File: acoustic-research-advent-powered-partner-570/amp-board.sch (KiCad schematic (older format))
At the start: 3 parts

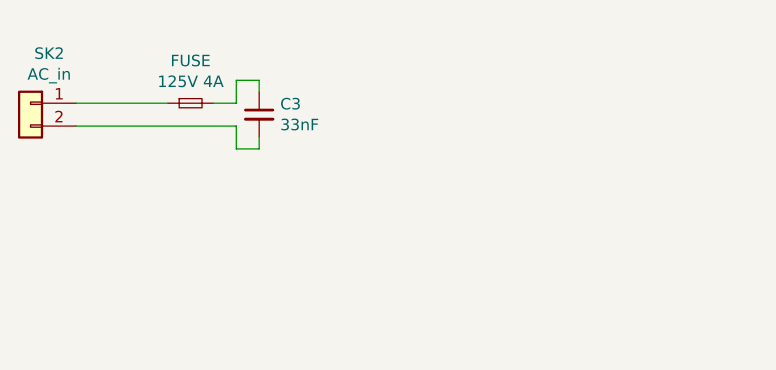
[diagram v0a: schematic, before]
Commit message: starting on the power input circuits
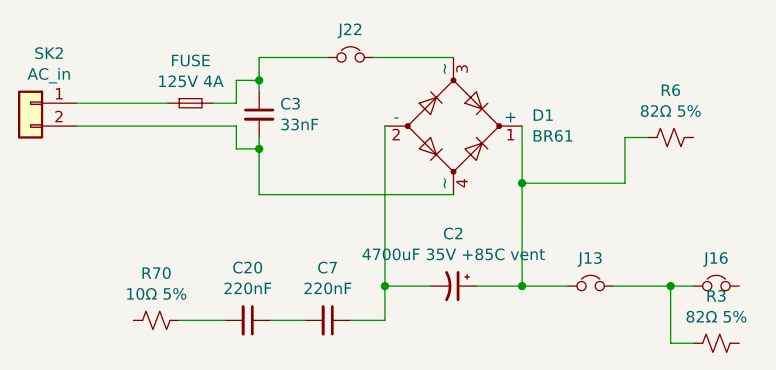
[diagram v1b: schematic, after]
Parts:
- added C2: 4700uF 35V +85C vent, symbol Device:CP1_Small
- added C20, C7: 220nF, symbol Device:C_Small
- added D1: BR61, symbol Device:D_Bridge_+-AA
- added J13, J16, J22: ~, symbol Device:Jumper_NC_Small
- added R3, R6: 82Ω 5%, symbol Device:R_Small_US
- added R70: 10Ω 5%, symbol Device:R_Small_US
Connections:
- net at C3.2, SK2.2 (Pin_2): now also D1.4 (~~)
- net at C3.1, FUSE.2: now also J22.1
- new net: C2.1, D1.1 (+), J13.1, R6.2
- new net: C2.2, C7.1, D1.2 (-)
- new net: D1.3 (~~), J22.2
- new net: C20.1, C7.2
- new net: J13.2, J16.1, R3.2
- new net: C20.2, R70.1
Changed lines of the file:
@@
 Wire Wire Line
 	1950 1500 1950 1450
+$Comp
+L Device:D_Bridge_+-AA D1
+U 1 1 5E8D387E
+P 2800 1400
+F 0 "D1" H 3144 1446 50  0000 L CNN
+F 1 "BR61" H 3144 1355 50  0000 L CNN
+F 2 "" H 2800 1400 50  0001 C CNN
+F 3 "~" H 2800 1400 50  0001 C CNN
+	1    2800 1400
+	1    0    0    -1
+$EndComp
+Wire Wire Line
+	1950 1200 1950 1100
+Wire Wire Line
+	1950 1100 2250 1100
+Connection ~ 1950 1200
+Wire Wire Line
+	1950 1500 1950 1700
+Wire Wire Line
+	1950 1700 2800 1700
+Connection ~ 1950 1500
+$Comp
+L Device:Jumper_NC_Small J22
+U 1 1 5E8D4B72
+P 2350 1100
+F 0 "J22" H 2350 1221 50  0000 C CNN
+F 1 "~" H 2350 1221 50  0000 C CNN
+F 2 "" H 2350 1100 50  0001 C CNN
+F 3 "~" H 2350 1100 50  0001 C CNN
+	1    2350 1100
+	1    0    0    -1
+$EndComp
+Wire Wire Line
+	2450 1100 2800 1100
+$Comp
+L Device:CP1_Small C2
+U 1 1 5E8D52A8
+P 2800 2100
+F 0 "C2" V 2572 2100 50  0000 C CNN
+F 1 "4700uF 35V +85C vent" V 2663 2100 50  0000 C CNN
+F 2 "" H 2800 2100 50  0001 C CNN
+F 3 "~" H 2800 2100 50  0001 C CNN
+	1    2800 2100
+	0    1    1    0
+$EndComp
+Wire Wire Line
+	2500 1400 2500 2100
+Wire Wire Line
+	2500 2100 2700 2100
+Wire Wire Line
+	3100 1400 3100 1650
+Wire Wire Line
+	3100 2100 2900 2100
+$Comp
+L Device:C_Small C7
+U 1 1 5E8D755A
+P 2250 2250
+F 0 "C7" V 2021 2250 50  0000 C CNN
+F 1 "220nF" V 2112 2250 50  0000 C CNN
+F 2 "" H 2250 2250 50  0001 C CNN
+F 3 "~" H 2250 2250 50  0001 C CNN
+	1    2250 2250
+	0    1    1    0
+$EndComp
+Wire Wire Line
+	2500 2100 2500 2250
+Wire Wire Line
+	2500 2250 2350 2250
+Connection ~ 2500 2100
+$Comp
+L Device:R_Small_US R6
+U 1 1 5E8D7F49
+P 3750 1450
+F 0 "R6" V 3545 1450 50  0000 C CNN
+F 1 "82Ω 5%" V 3636 1450 50  0000 C CNN
+F 2 "" H 3750 1450 50  0001 C CNN
+F 3 "~" H 3750 1450 50  0001 C CNN
+	1    3750 1450
+	0    1    1    0
+$EndComp
+Wire Wire Line
+	3100 1650 3550 1650
+Wire Wire Line
+	3550 1650 3550 1450
+Wire Wire Line
+	3550 1450 3650 1450
+Connection ~ 3100 1650
+Wire Wire Line
+	3100 1650 3100 2100
+$Comp
+L Device:Jumper_NC_Small J13
+U 1 1 5E8D8BA6
+P 3400 2100
+F 0 "J13" H 3400 2221 50  0000 C CNN
+F 1 "~" H 3400 2221 50  0000 C CNN
+F 2 "" H 3400 2100 50  0001 C CNN
+F 3 "~" H 3400 2100 50  0001 C CNN
+	1    3400 2100
+	1    0    0    -1
+$EndComp
+Wire Wire Line
+	3100 2100 3300 2100
+Connection ~ 3100 2100
+$Comp
+L Device:C_Small C20
+U 1 1 5E8D9A58
+P 1900 2250
+F 0 "C20" V 1671 2250 50  0000 C CNN
+F 1 "220nF" V 1762 2250 50  0000 C CNN
+F 2 "" H 1900 2250 50  0001 C CNN
+F 3 "~" H 1900 2250 50  0001 C CNN
+	1    1900 2250
+	0    1    1    0
+$EndComp
+Wire Wire Line
+	2000 2250 2150 2250
+$Comp
+L Device:R_Small_US R70
+U 1 1 5E8DA32F
+P 1500 2250
+F 0 "R70" V 1295 2250 50  0000 C CNN
+F 1 "10Ω 5%" V 1386 2250 50  0000 C CNN
+F 2 "" H 1500 2250 50  0001 C CNN
+F 3 "~" H 1500 2250 50  0001 C CNN
+	1    1500 2250
+	0    1    1    0
+$EndComp
+Wire Wire Line
+	1600 2250 1800 2250
+$Comp
+L Device:Jumper_NC_Small J16
+U 1 1 5E8DAF35
+P 3950 2100
+F 0 "J16" H 3950 2221 50  0000 C CNN
+F 1 "~" H 3950 2221 50  0000 C CNN
+F 2 "" H 3950 2100 50  0001 C CNN
+F 3 "~" H 3950 2100 50  0001 C CNN
+	1    3950 2100
+	1    0    0    -1
+$EndComp
+$Comp
+L Device:R_Small_US R3
+U 1 1 5E8DB2C5
+P 3950 2350
+F 0 "R3" V 3745 2350 50  0000 C CNN
+F 1 "82Ω 5%" V 3836 2350 50  0000 C CNN
+F 2 "" H 3950 2350 50  0001 C CNN
+F 3 "~" H 3950 2350 50  0001 C CNN
+	1    3950 2350
+	0    1    1    0
+$EndComp
+Wire Wire Line
+	3850 2100 3750 2100
+Wire Wire Line
+	3750 2100 3750 2350
+Wire Wire Line
+	3750 2350 3850 2350
+Wire Wire Line
+	3500 2100 3750 2100
+Connection ~ 3750 2100
 $EndSCHEMATC

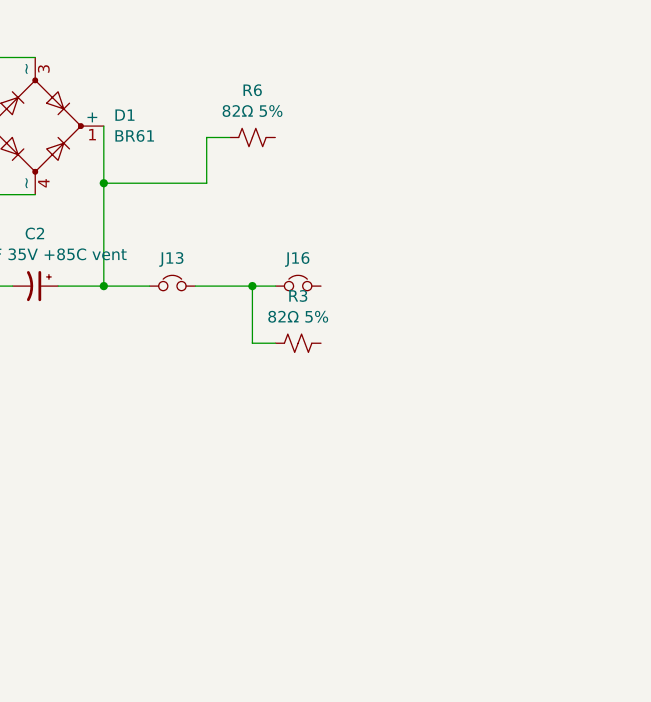
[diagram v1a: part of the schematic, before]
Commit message: more transistors
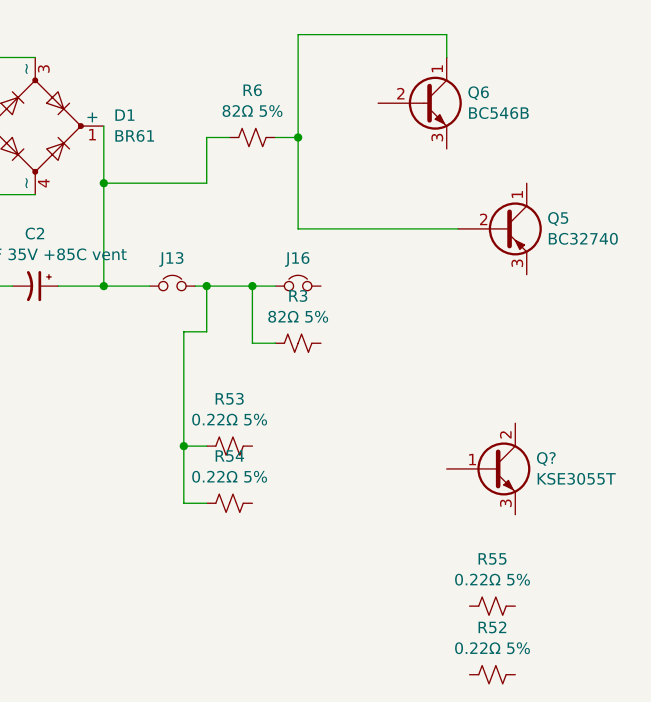
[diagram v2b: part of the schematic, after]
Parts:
- added Q5: BC32740, Package_TO_SOT_THT:TO-92_Inline, symbol Transistor_BJT:BC327
- added Q6: BC546B, Package_TO_SOT_THT:TO-92_Inline, symbol Transistor_BJT:BC546
- added Q?: KSE3055T, symbol Device:Q_NPN_BCE
- added R52, R53, R54, R55: 0.22Ω 5%, symbol Device:R_Small_US
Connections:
- net at R6.1: now also Q5.2 (B), Q6.1 (C)
- net at J13.2, J16.1, R3.2: now also R53.2, R54.2
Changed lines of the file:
@@
 	3750 2350 3850 2350
 Wire Wire Line
-	3500 2100 3750 2100
+	3500 2100 3550 2100
 Connection ~ 3750 2100
+$Comp
+L Transistor_BJT:BC546 Q6
+U 1 1 5E8DC9B8
+P 4500 1300
+F 0 "Q6" H 4691 1346 50  0000 L CNN
+F 1 "BC546B" H 4691 1255 50  0000 L CNN
+F 2 "Package_TO_SOT_THT:TO-92_Inline" H 4700 1225 50  0001 L CIN
+F 3 "http://www.fairchildsemi.com/ds/BC/BC547.pdf" H 4500 1300 50  0001 L CNN
+	1    4500 1300
+	1    0    0    -1
+$EndComp
+Wire Wire Line
+	3850 1450 3950 1450
+Wire Wire Line
+	3950 1450 3950 1000
+Wire Wire Line
+	3950 1000 4600 1000
+Wire Wire Line
+	4600 1000 4600 1100
+$Comp
+L Transistor_BJT:BC327 Q5
+U 1 1 5E8DDD31
+P 4850 1850
+F 0 "Q5" H 5040 1896 50  0000 L CNN
+F 1 "BC32740" H 5040 1805 50  0000 L CNN
+F 2 "Package_TO_SOT_THT:TO-92_Inline" H 5050 1775 50  0001 L CIN
+F 3 "http://www.onsemi.com/pub_link/Collateral/BC327-D.PDF" H 4850 1850 50  0001 L CNN
+	1    4850 1850
+	1    0    0    -1
+$EndComp
+Wire Wire Line
+	3950 1450 3950 1850
+Wire Wire Line
+	3950 1850 4650 1850
+Connection ~ 3950 1450
+$Comp
+L Device:R_Small_US R53
+U 1 1 5E8DEE3E
+P 3650 2800
+F 0 "R53" V 3445 2800 50  0000 C CNN
+F 1 "0.22Ω 5%" V 3536 2800 50  0000 C CNN
+F 2 "" H 3650 2800 50  0001 C CNN
+F 3 "~" H 3650 2800 50  0001 C CNN
+	1    3650 2800
+	0    1    1    0
+$EndComp
+$Comp
+L Device:R_Small_US R54
+U 1 1 5E8DF44C
+P 3650 3050
+F 0 "R54" V 3445 3050 50  0000 C CNN
+F 1 "0.22Ω 5%" V 3536 3050 50  0000 C CNN
+F 2 "" H 3650 3050 50  0001 C CNN
+F 3 "~" H 3650 3050 50  0001 C CNN
+	1    3650 3050
+	0    1    1    0
+$EndComp
+$Comp
+L Device:R_Small_US R55
+U 1 1 5E8DFA91
+P 4800 3500
+F 0 "R55" V 4595 3500 50  0000 C CNN
+F 1 "0.22Ω 5%" V 4686 3500 50  0000 C CNN
+F 2 "" H 4800 3500 50  0001 C CNN
+F 3 "~" H 4800 3500 50  0001 C CNN
+	1    4800 3500
+	0    1    1    0
+$EndComp
+$Comp
+L Device:R_Small_US R52
+U 1 1 5E8DFF45
+P 4800 3800
+F 0 "R52" V 4595 3800 50  0000 C CNN
+F 1 "0.22Ω 5%" V 4686 3800 50  0000 C CNN
+F 2 "" H 4800 3800 50  0001 C CNN
+F 3 "~" H 4800 3800 50  0001 C CNN
+	1    4800 3800
+	0    1    1    0
+$EndComp
+Wire Wire Line
+	3550 2800 3450 2800
+Wire Wire Line
+	3450 2800 3450 3050
+Wire Wire Line
+	3450 3050 3550 3050
+Wire Wire Line
+	3450 2800 3450 2300
+Wire Wire Line
+	3450 2300 3550 2300
+Wire Wire Line
+	3550 2300 3550 2100
+Connection ~ 3450 2800
+Connection ~ 3550 2100
+Wire Wire Line
+	3550 2100 3750 2100
+$Comp
+L Device:Q_NPN_BCE Q?
+U 1 1 5E8E7157
+P 4800 2900
+F 0 "Q?" H 4991 2946 50  0000 L CNN
+F 1 "KSE3055T" H 4991 2855 50  0000 L CNN
+F 2 "" H 5000 3000 50  0001 C CNN
+F 3 "~" H 4800 2900 50  0001 C CNN
+	1    4800 2900
+	1    0    0    -1
+$EndComp
 $EndSCHEMATC

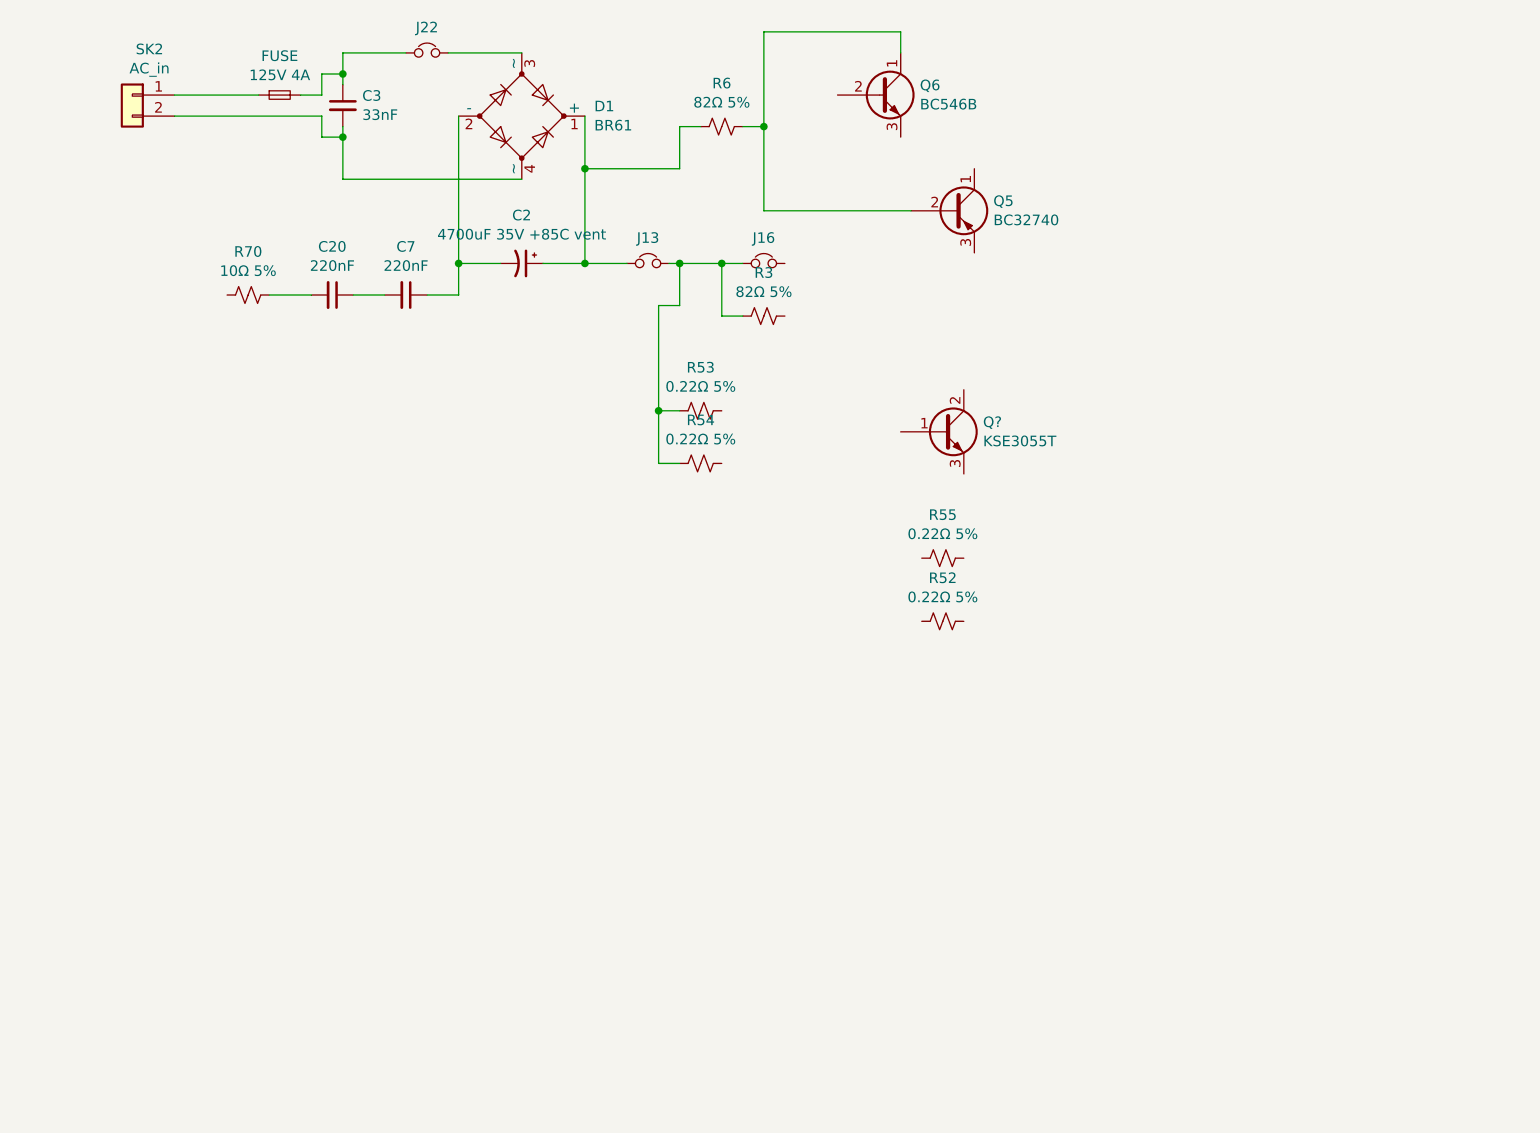
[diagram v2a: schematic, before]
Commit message: added all transistors
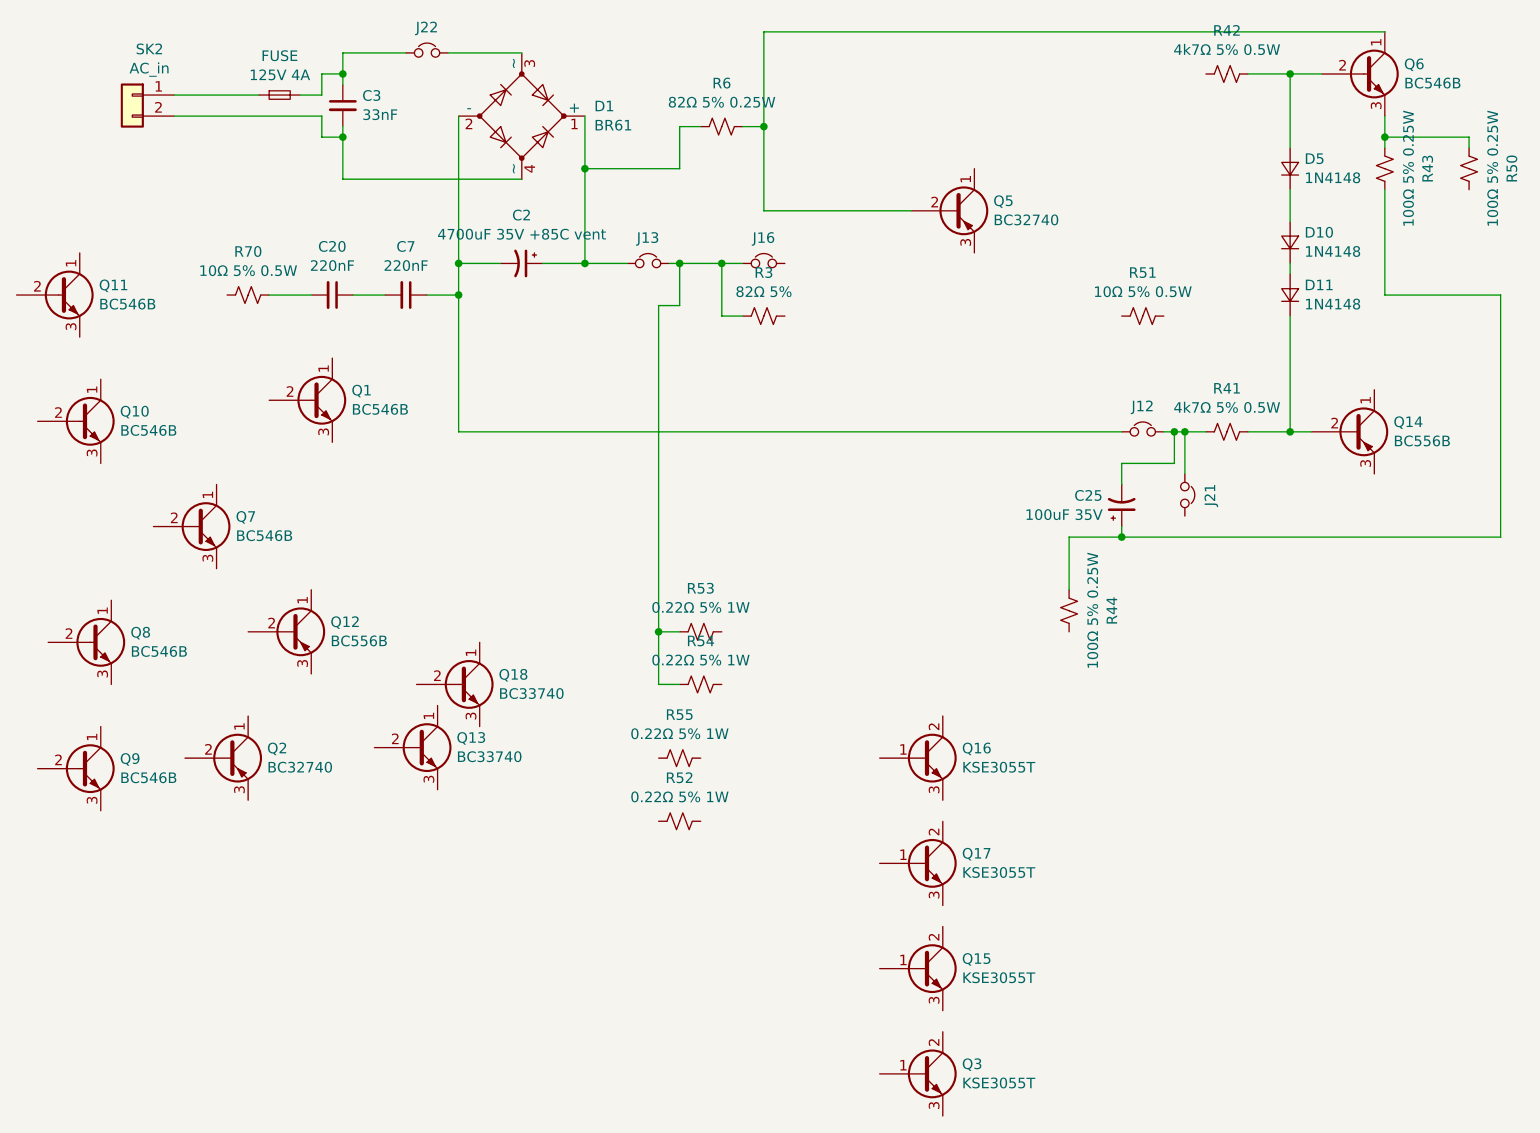
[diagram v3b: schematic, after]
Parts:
- added C25: 100uF 35V, symbol Device:CP1_Small
- added D10, D11, D5: 1N4148, symbol Device:D_Small
- added J12, J21: ~, symbol Device:Jumper_NC_Small
- added Q1, Q10, Q11, Q7, Q8, Q9: BC546B, Package_TO_SOT_THT:TO-92_Inline, symbol Transistor_BJT:BC546
- added Q12, Q14: BC556B, Package_TO_SOT_THT:TO-92_Inline, symbol Transistor_BJT:BC556
- added Q13, Q18: BC33740, Package_TO_SOT_THT:TO-92_Inline, symbol Transistor_BJT:BC337
- added Q15, Q17, Q3: KSE3055T, TO-220-3, symbol Device:Q_NPN_BCE
- added Q2: BC32740, Package_TO_SOT_THT:TO-92_Inline, symbol Transistor_BJT:BC327
- added R41, R42: 4k7Ω 5% 0.5W, symbol Device:R_Small_US
- added R43, R44, R50: 100Ω 5% 0.25W, symbol Device:R_Small_US
- added R51: 10Ω 5% 0.5W, symbol Device:R_Small_US
- Q16: renamed from Q?; footprint (none) -> TO-220-3
- R52, R53, R54, R55: value 0.22Ω 5% -> 0.22Ω 5% 1W
- R6: value 82Ω 5% -> 82Ω 5% 0.25W
- R70: value 10Ω 5% -> 10Ω 5% 0.5W
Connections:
- net at C2.2, C7.1, D1.2 (-): now also J12.1
- net at Q6.2 (B): now also D5.2 (A), R42.1
- net at Q6.3 (E): now also R43.2, R50.2
- new net: D11.1 (K), Q14.2 (B), R41.1
- new net: C25.1, R43.1, R44.2
- new net: D10.2 (A), D5.1 (K)
- new net: D10.1 (K), D11.2 (A)
- new net: C25.2, J12.2, J21.1, R41.2
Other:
- moved on the sheet: Q16, Q6, R52, R53, R54, R55

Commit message: first op amp
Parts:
- added J10: ~, symbol Device:Jumper_NC_Small
- added R45: 100Ω 5% 0.25W, symbol Device:R_Small_US
- added R61: 39kΩ 2% 0.25W, symbol Device:R_Small_US
- added U? (x3): NJM4556A, symbol Amplifier_Operational:NJM4556A
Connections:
- net at Q14.3 (E): now also R44.1, R45.1
- net at R50.1: now also R45.2, R61.2
- new net: J10.1, R61.1
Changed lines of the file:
@@
 Wire Wire Line
 	6900 1500 6900 1550
+$Comp
+L Device:R_Small_US R61
+U 1 1 5E9611AB
+P 7800 2150
+F 0 "R61" V 7595 2150 50  0000 C CNN
+F 1 "39kΩ 2% 0.25W" V 7686 2150 50  0000 C CNN
+F 2 "" H 7800 2150 50  0001 C CNN
+F 3 "~" H 7800 2150 50  0001 C CNN
+	1    7800 2150
+	-1   0    0    1
+$EndComp
+Wire Wire Line
+	7300 1750 7300 1850
+Wire Wire Line
+	7300 1850 7800 1850
+Wire Wire Line
+	7800 1850 7800 1900
+$Comp
+L Device:R_Small_US R45
+U 1 1 5E9675B4
+P 8350 2150
+F 0 "R45" V 8145 2150 50  0000 C CNN
+F 1 "100Ω 5% 0.25W" V 8236 2150 50  0000 C CNN
+F 2 "" H 8350 2150 50  0001 C CNN
+F 3 "~" H 8350 2150 50  0001 C CNN
+	1    8350 2150
+	-1   0    0    1
+$EndComp
+Wire Wire Line
+	7800 1900 8350 1900
+Wire Wire Line
+	8350 1900 8350 2050
+Connection ~ 7800 1900
+Wire Wire Line
+	7800 1900 7800 2050
+Wire Wire Line
+	8350 2250 8350 4050
+Wire Wire Line
+	8350 4050 6850 4050
+Wire Wire Line
+	5400 4050 5400 3850
+Wire Wire Line
+	6850 3100 6850 4050
+Connection ~ 6850 4050
+Wire Wire Line
+	6850 4050 5400 4050
+$Comp
+L Device:Jumper_NC_Small J10
+U 1 1 5E96DA6D
+P 7800 2550
+F 0 "J10" H 7800 2671 50  0000 C CNN
+F 1 "~" H 7800 2671 50  0000 C CNN
+F 2 "" H 7800 2550 50  0001 C CNN
+F 3 "~" H 7800 2550 50  0001 C CNN
+	1    7800 2550
+	0    1    1    0
+$EndComp
+Wire Wire Line
+	7800 2450 7800 2250
+$Comp
+L Amplifier_Operational:NJM4556A U?
+U 1 1 5E972E09
+P 7500 4550
+F 0 "U?" H 7500 4917 50  0000 C CNN
+F 1 "NJM4556A" H 7500 4826 50  0000 C CNN
+F 2 "" H 7500 4550 50  0001 C CNN
+F 3 "http://www.njr.com/semicon/PDF/NJM4556A_E.pdf" H 7500 4550 50  0001 C CNN
+	1    7500 4550
+	1    0    0    -1
+$EndComp
+$Comp
+L Amplifier_Operational:NJM4556A U?
+U 2 1 5E97436F
+P 8750 4700
+F 0 "U?" H 8750 5067 50  0000 C CNN
+F 1 "NJM4556A" H 8750 4976 50  0000 C CNN
+F 2 "" H 8750 4700 50  0001 C CNN
+F 3 "http://www.njr.com/semicon/PDF/NJM4556A_E.pdf" H 8750 4700 50  0001 C CNN
+	2    8750 4700
+	1    0    0    -1
+$EndComp
+$Comp
+L Amplifier_Operational:NJM4556A U?
+U 3 1 5E975638
+P 6400 4650
+F 0 "U?" H 6358 4696 50  0000 L CNN
+F 1 "NJM4556A" H 6358 4605 50  0000 L CNN
+F 2 "" H 6400 4650 50  0001 C CNN
+F 3 "http://www.njr.com/semicon/PDF/NJM4556A_E.pdf" H 6400 4650 50  0001 C CNN
+	3    6400 4650
+	1    0    0    -1
+$EndComp
 $EndSCHEMATC
